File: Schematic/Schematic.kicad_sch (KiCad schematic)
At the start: 18 parts, among them J1 S2B-PH-K-S_LF__SN_, J2 Conn_02x08_Odd_Even, P1 282837-2, P2 282837-2, U1 NRF52840-DONGLE, U2 L293D, U3 LM1117DT-3.3, U4 YAAJ_DCDC_StepDown_LM2596

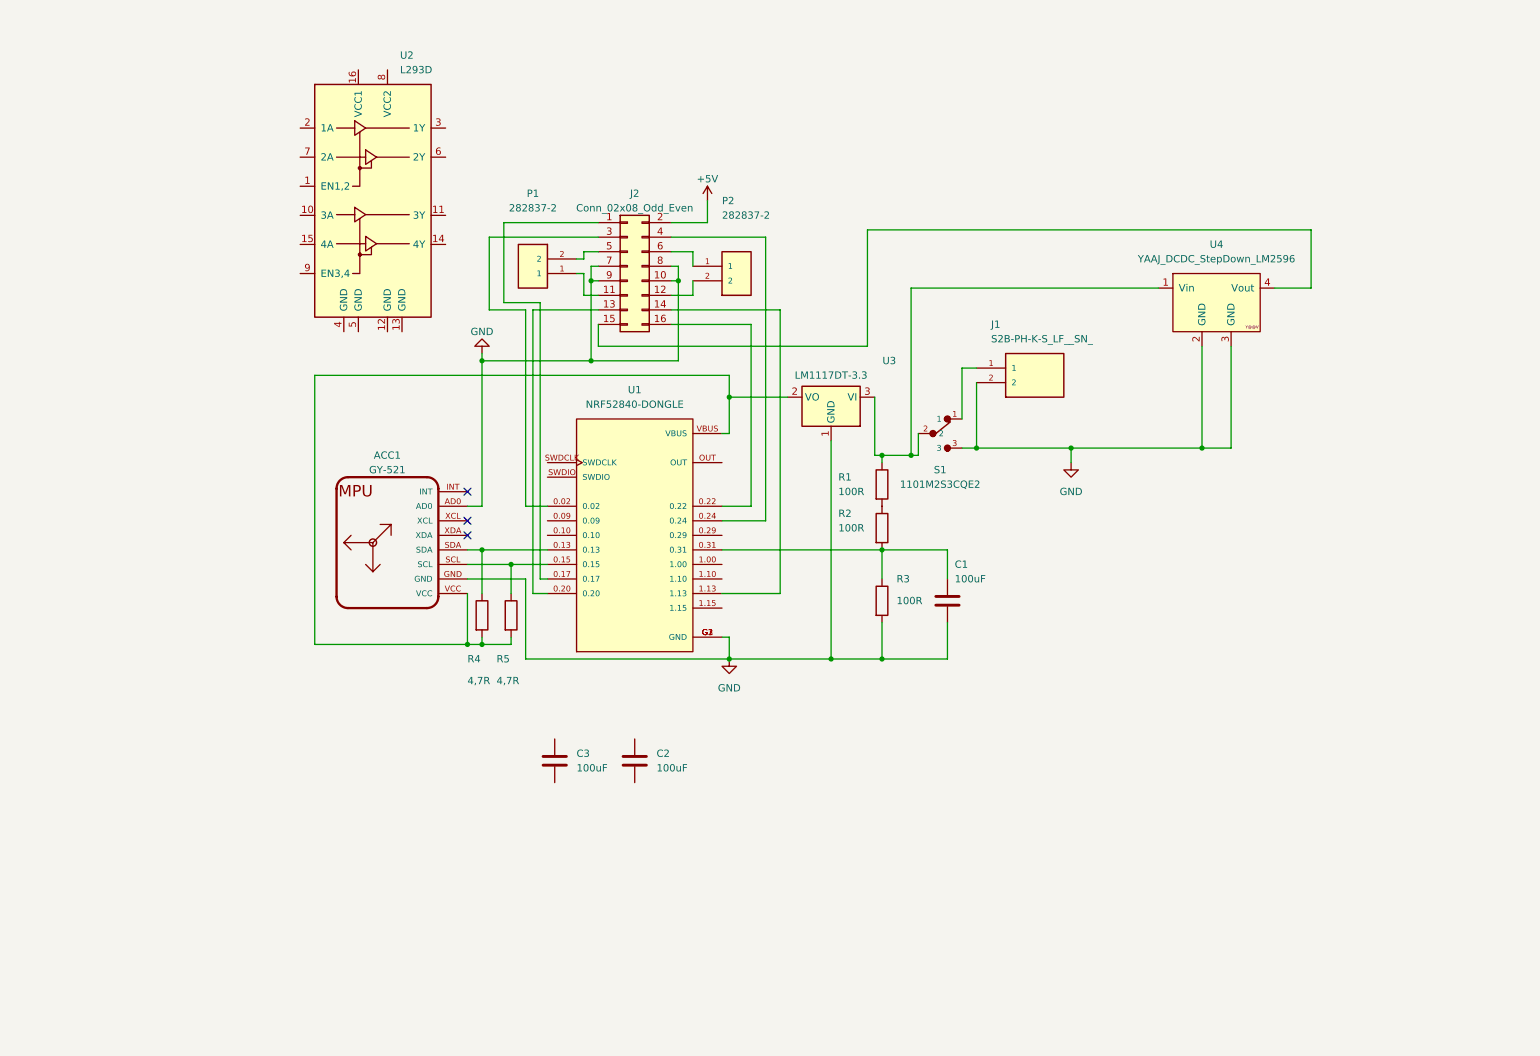
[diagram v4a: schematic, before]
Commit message: PCB: completing the electrical diagram
-fix with the H bridge (we have to use TB6612FNG which can operate at PWM 3.3 V
-complete schematic
-create prototype PCB schematic
-track PCB paths
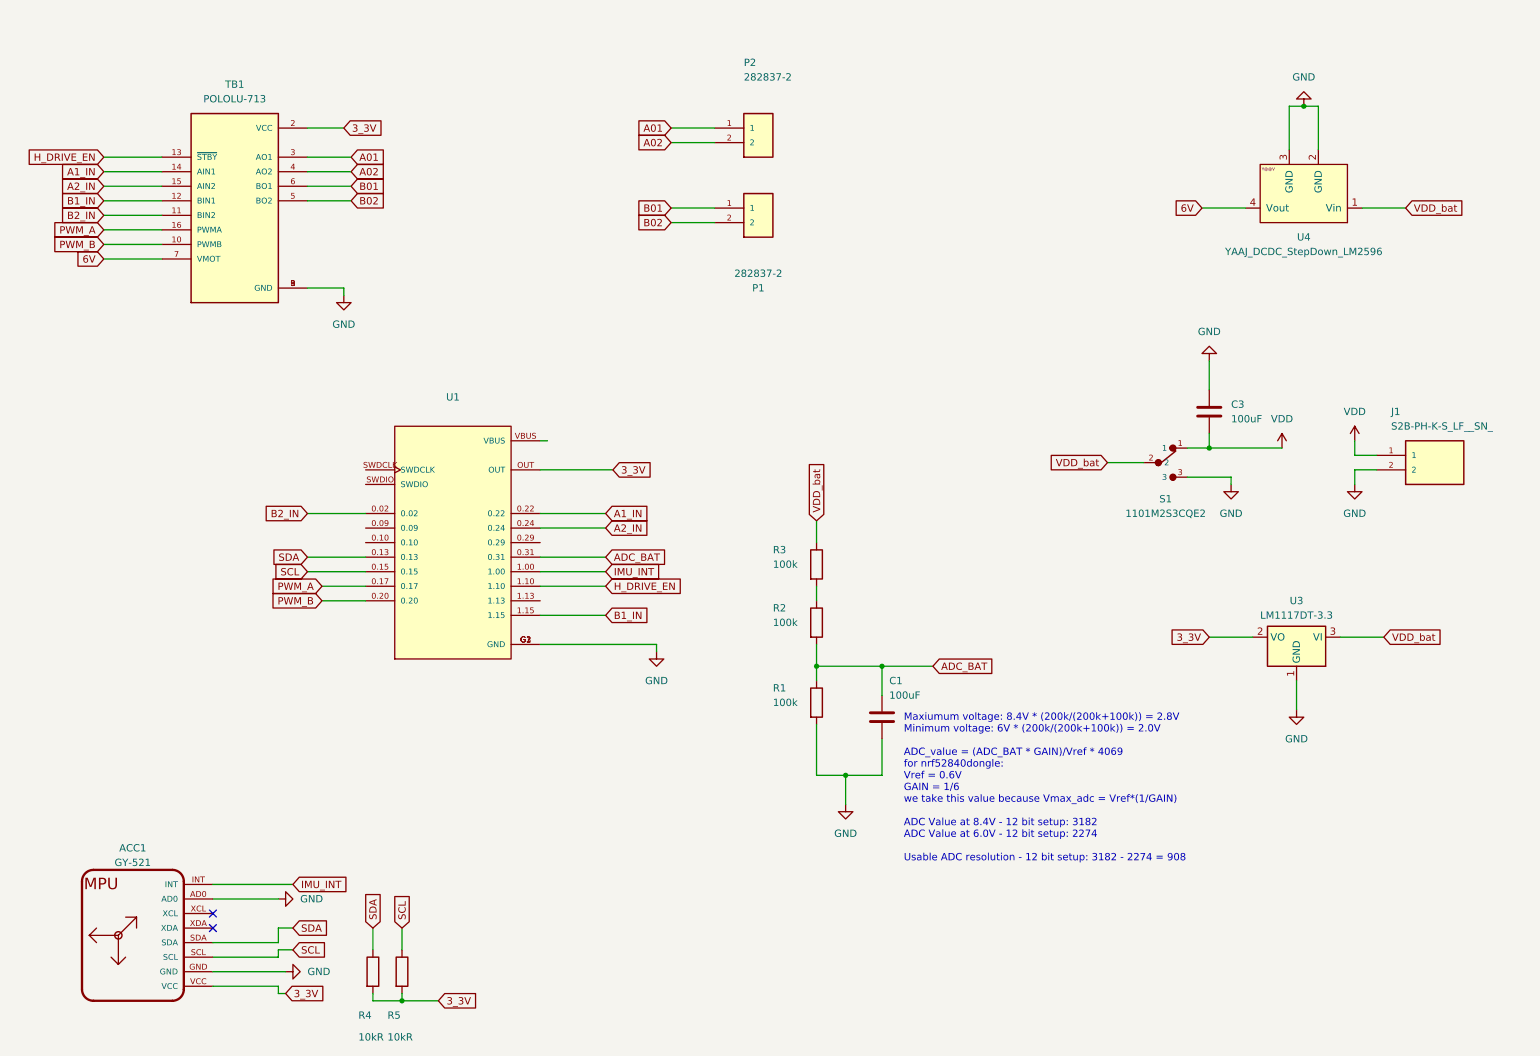
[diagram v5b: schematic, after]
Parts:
- removed C2: 100uF, Capacitor_THT:C_Disc_D7.5mm_W4.4mm_P5.00mm, symbol Device:C
- removed J2: Conn_02x08_Odd_Even, Package_DIP:DIP-16_W10.16mm, symbol Connector_Generic:Conn_02x08_Odd_Even
- removed U2: L293D, Package_DIP:DIP-16_W7.62mm, symbol Driver_Motor:L293D
- added TB1: POLOLU-713, POLOLU-713:SHIELD_POLOLU-713, symbol POLOLU-713:POLOLU-713
- R1, R2, R3: value 100R -> 100k
- R4, R5: value 4,7R -> 10kR
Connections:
- net GND: now also C3.1, R1.2, TB1.1 (GND), TB1.8 (GND), TB1.9 (GND); no longer R3.2
- net VDD: now reaches C3.2
- net VDD: now also J1.1, S1.1
- net B2_IN: now reaches U1.0.02
- net B2_IN: now also TB1.11 (BIN2)
- net SDA: now reaches ACC1.SDA, R4.1, U1.0.13
- net SCL: now reaches ACC1.SCL, R5.1, U1.0.15
- net PWM_A: now reaches U1.0.17
- net PWM_A: now also TB1.16 (PWMA)
- net PWM_B: now reaches U1.0.20
- net PWM_B: now also TB1.10 (PWMB)
- net A1_IN: now reaches U1.0.22
- net A1_IN: now also TB1.14 (AIN1)
- net A2_IN: now reaches U1.0.24
- net A2_IN: now also TB1.15 (AIN2)
- net ADC_BAT: now reaches C1.1, R2.2, U1.0.31
- net ADC_BAT: now also R1.1; no longer R3.1
- net IMU_INT: now reaches U1.1.00
- net IMU_INT: now also ACC1.INT
- net H_DRIVE_EN: now reaches U1.1.10
- net H_DRIVE_EN: now also TB1.13 (~{STBY})
- net B1_IN: now reaches U1.1.15
- net B1_IN: now also TB1.12 (BIN1)
- net 3_3V: now reaches U1.OUT
- net 3_3V: now also ACC1.VCC, R4.2, R5.2, U3.2 (VO), TB1.2 (VCC)
- net B01: now reaches P1.1
- net B01: now also TB1.6 (BO1)
- net B02: now reaches P1.2
- net B02: now also TB1.5 (BO2)
- net A01: now reaches P2.1
- net A01: now also TB1.3 (AO1)
- net A02: now reaches P2.2
- net A02: now also TB1.4 (AO2)
- net VDD_bat: now reaches S1.2, U3.3 (VI), U4.1 (Vin)
- net VDD_bat: now also R3.1; no longer R1.1
- net 6V: now reaches U4.4 (Vout)
- net 6V: now also TB1.7 (VMOT)
- net at R2.1: now also R3.2; no longer R1.2
- now unconnected: U1.VBUS
- no-connect marks 3 -> 2
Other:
- note added: "Maxiumum voltage: 8.4V * (200k/(200k+100k)) = 2.8V Minimum voltage: 6V * (200k/(200k+100k)) = 2.0V ADC_value = (ADC_BAT * GAIN)/Vref * 4069 for nrf52840dongle: Vref = 0.6V GAIN = 1/6 we take this value because Vmax_adc = Vref*(1/GAIN) ADC Value at 8.4V - 12 bit setup: 3182 ADC Value at 6.0V - 12 bit setup: 2274 Usable ADC resolution - 12 bit setup: 3182 - 2274 = 908"
- moved on the sheet: ACC1, C1, C3, J1, P1, P2, R2, R4, R5, S1, U1, U3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
